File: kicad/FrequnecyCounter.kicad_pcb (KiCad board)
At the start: 4 copper layers, 130 x 90 mm, 144 parts, among them J1 USB_B, J2 CONN_COAXIAL, J3 CONN_COAXIAL, J4 CONN_COAXIAL, Q1 BC846B, T1 WBC16-1T, U1 TPS650250, U10 MC12093, U11 tx176, U12 TLV3501, U2 LP3871, U3 MCP4725, U4 NFM18PS, U5 WE-TVS-824011, U6 FT2232D, U7 6MHz_Crystal, U8 AT93C46DN-SH, U9 LTC6957-3, X1 Stiftleiste_2x10Pm_R2.54

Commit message: Changed some component values to increase the fit & Changed power-supply of the eeprom to use the PWR_EN of the FT2232D
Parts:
- removed REF** (x15): VIA-0.6mm, Footprints_LJ:VIA-0.6mm
- C48: value 1n -> 100p
- C51: value 100p -> 47p
- L2: footprint LPS5030 -> Footprints_LJ:LPS5030
- R17, R22: value 680R -> 2k
- U11: footprint tx176 -> Footprints_LJ:tx176
- U7: footprint Crystal_SMD_HC49-SD -> Crystals:Crystal_SMD_HC49-SD
- moved R12 5.32 mm to (100.7, 137.7), turned to 0 degrees
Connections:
- C42 pad 1: +3V3 -> +5V
- R12 pad 2: +3V3 -> +5V
- R28 pad 1: +3V3 -> +5V
- U8 pad 6: +3V3 -> +5V
- U8 pad 8: +3V3 -> +5V
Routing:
- net +5V: track 132.3 -> 173.7 mm, vias 6 -> 9
- net +3V3: track 90.9 -> 79.7 mm, vias 28 -> 25
- net GND: track 11.3 -> 18.3 mm, vias 6 -> 19
- net (no net): vias 205 -> 172

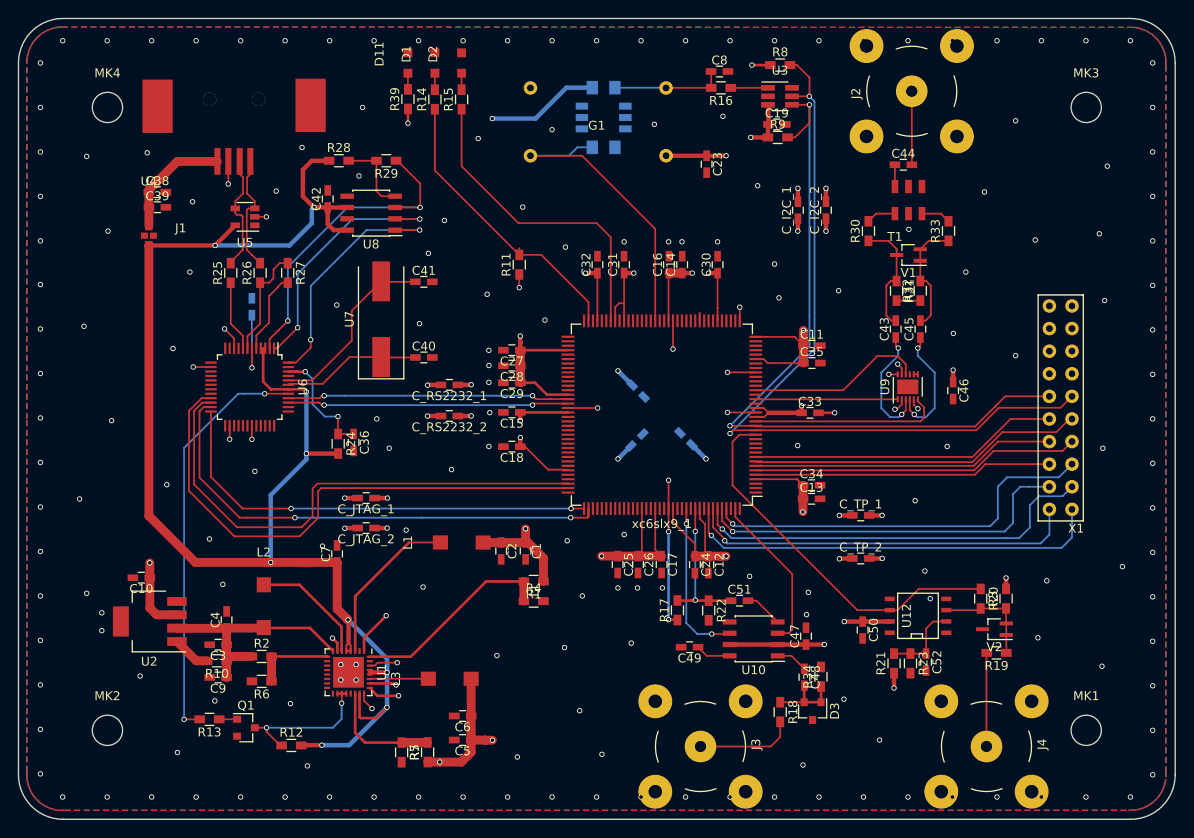
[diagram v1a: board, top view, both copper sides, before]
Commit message: clean up in layout & add exports (assembly drawings)
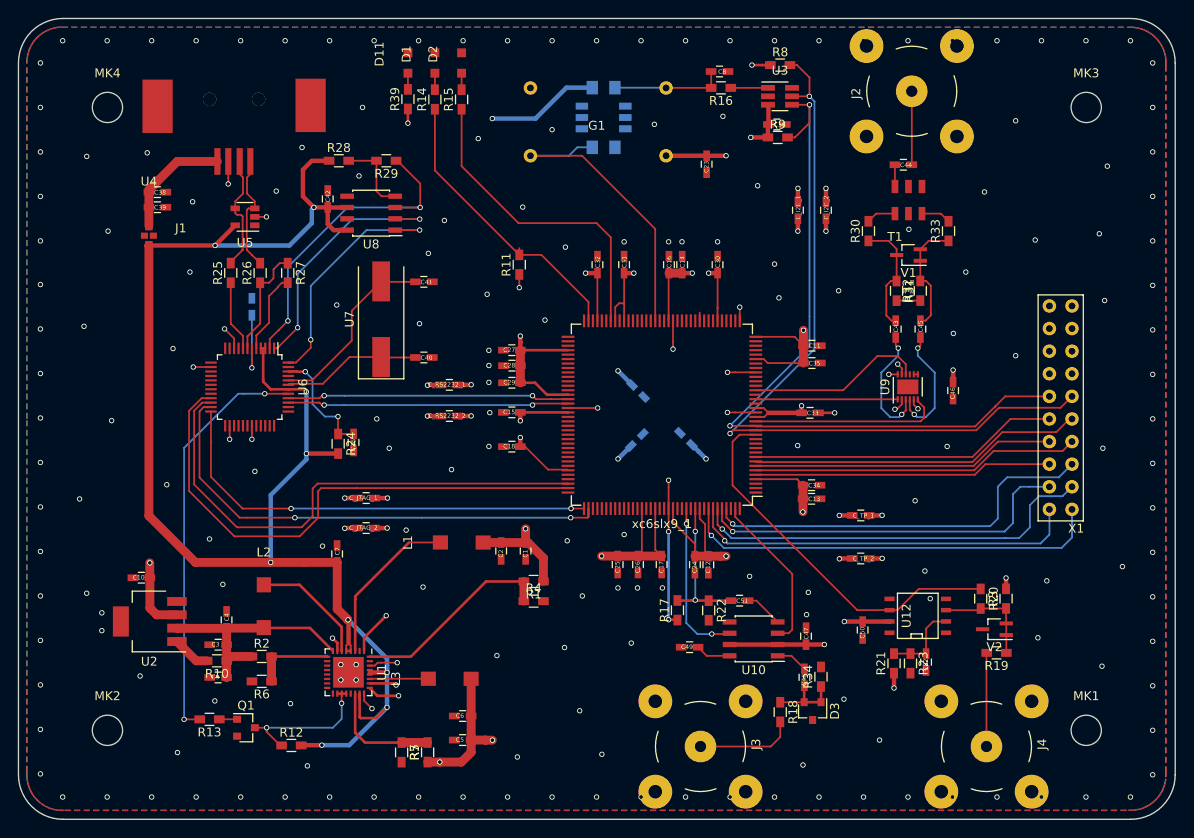
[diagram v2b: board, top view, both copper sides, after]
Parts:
- C1, C10, C11, C12, C13, C14, C15, C16, C17, C18, C19, C2, C20, C21, C22, C23, C24, C25, C26, C27, C28, C29, C3, C30, C31, C32, C33, C34, C35, C36, C37, C38, C39, C4, C40, C41, C42, C43, C44, C45, C46, C47, C48, C49, C5, C50, C51, C52, C6, C7, C8, C9, C_I2C_1, C_I2C_2, C_JTAG_1, C_JTAG_2, C_RS2232_1, C_RS2232_2, C_TP_1, C_TP_2: footprint Capacitors_SMD:C_0603_HandSoldering -> Footprints_LJ:Cap_0603_HandSoldering_1
